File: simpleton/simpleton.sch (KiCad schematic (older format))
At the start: 57 parts

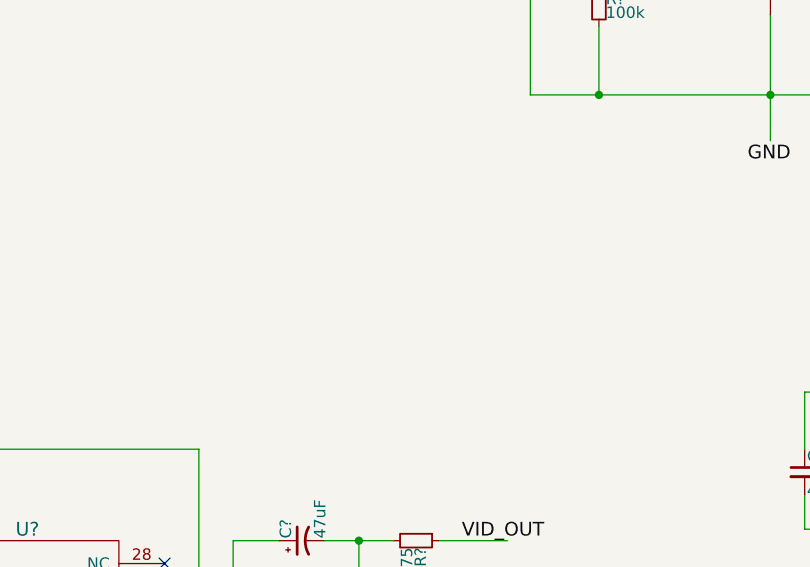
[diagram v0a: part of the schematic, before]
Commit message: Added vid ports and spek sat power port
Closes #13
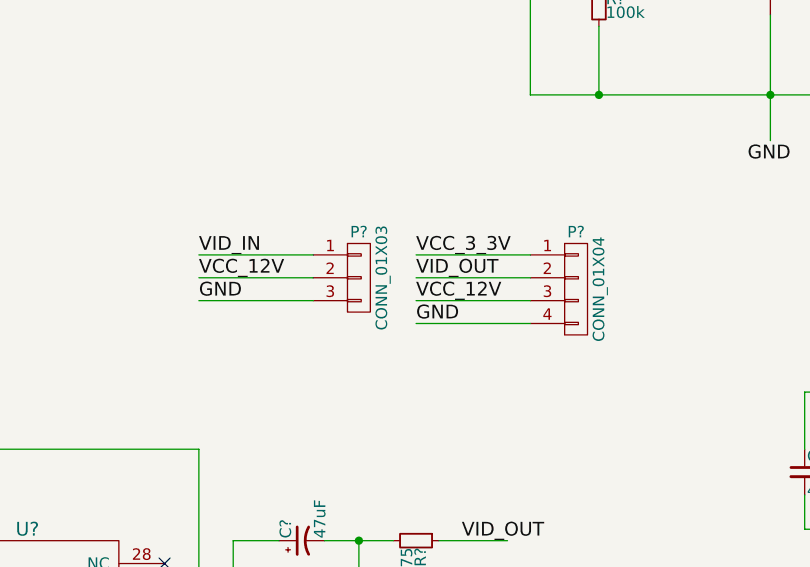
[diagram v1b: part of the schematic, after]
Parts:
- added P?: CONN_01X04, symbol CONN_01X04
- added P?: CONN_01X03, symbol CONN_01X03
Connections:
- net labels added: VCC_12V
- wire segments 228 -> 235
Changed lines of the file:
@@
 Text Label 800  1500 0    60   ~ 0
 U4_INV
+$Comp
+L CONN_01X04 P?
+U 1 1 56D50EB3
+P 11950 8350
+F 0 "P?" H 11950 8600 50  0000 C CNN
+F 1 "CONN_01X04" V 12050 8350 50  0000 C CNN
+F 2 "" H 11950 8350 60  0000 C CNN
+F 3 "" H 11950 8350 60  0000 C CNN
+	1    11950 8350
+	1    0    0    -1
+$EndComp
+Wire Wire Line
+	11750 8200 11250 8200
+Wire Wire Line
+	11750 8300 11250 8300
+Wire Wire Line
+	11750 8400 11250 8400
+Wire Wire Line
+	11750 8500 11250 8500
+Text Label 11250 8500 0    60   ~ 0
+GND
+Text Label 11250 8400 0    60   ~ 0
+VCC_12V
+Text Label 11250 8300 0    60   ~ 0
+VID_OUT
+Text Label 11250 8200 0    60   ~ 0
+VCC_3_3V
+$Comp
+L CONN_01X03 P?
+U 1 1 56D51B48
+P 11000 8300
+F 0 "P?" H 11000 8500 50  0000 C CNN
+F 1 "CONN_01X03" V 11100 8300 50  0000 C CNN
+F 2 "" H 11000 8300 60  0000 C CNN
+F 3 "" H 11000 8300 60  0000 C CNN
+	1    11000 8300
+	1    0    0    -1
+$EndComp
+Wire Wire Line
+	10800 8400 10300 8400
+Wire Wire Line
+	10800 8300 10300 8300
+Wire Wire Line
+	10800 8200 10300 8200
+Text Label 10300 8400 0    60   ~ 0
+GND
+Text Label 10300 8300 0    60   ~ 0
+VCC_12V
+Text Label 10300 8200 0    60   ~ 0
+VID_IN
 $EndSCHEMATC

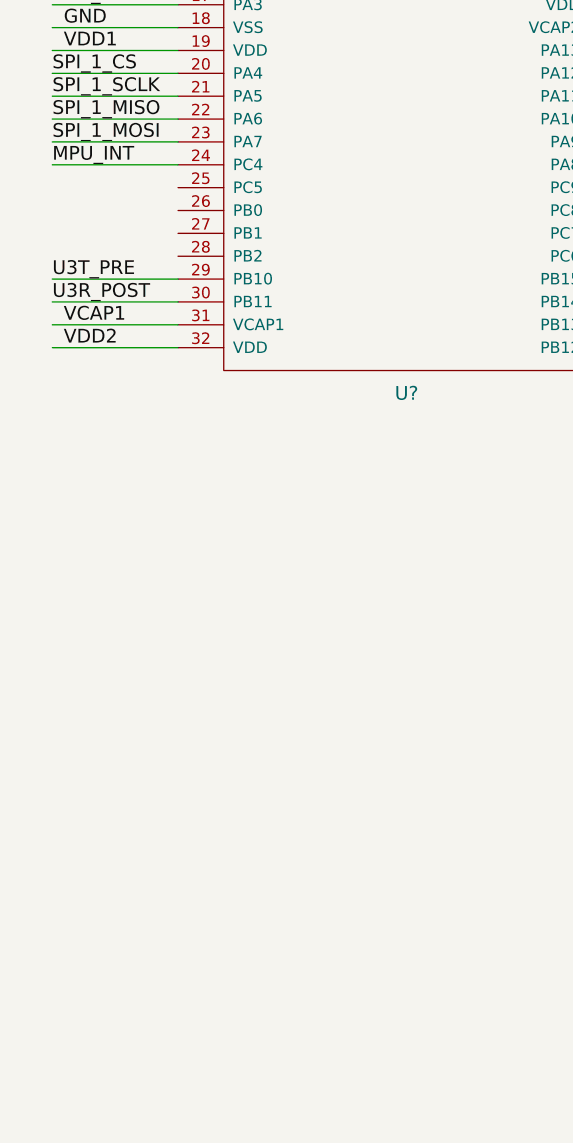
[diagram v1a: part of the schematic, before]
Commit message: Added ESC outputs
Closes #9
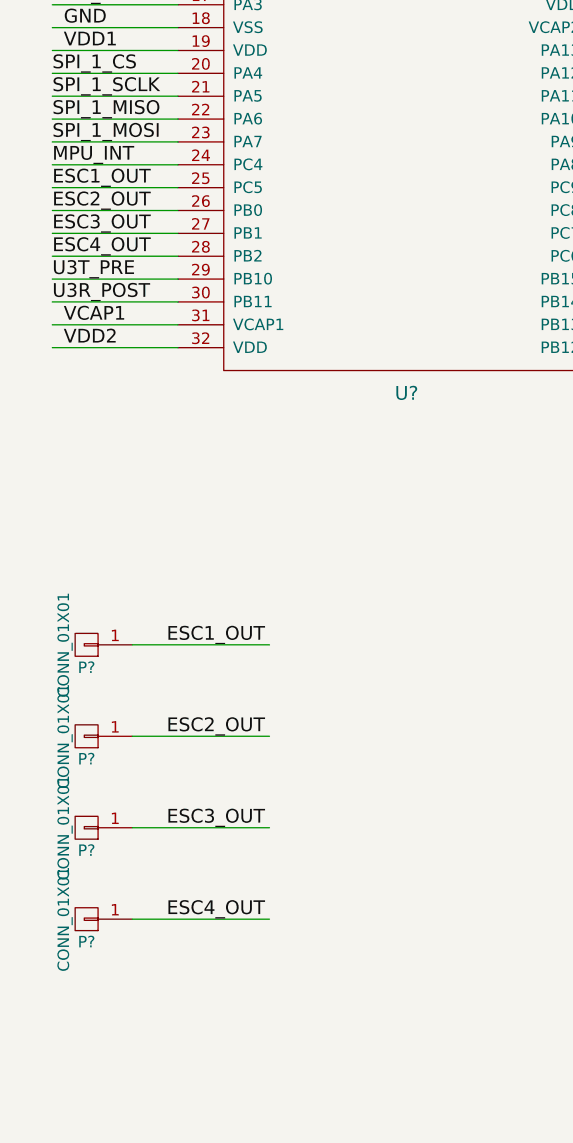
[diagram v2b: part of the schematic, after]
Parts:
- added P? (x4): CONN_01X01, symbol CONN_01X01
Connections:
- net labels added: ESC1_OUT, ESC2_OUT, ESC3_OUT, ESC4_OUT
- wire segments 235 -> 243
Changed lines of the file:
@@
 Text Label 10300 8200 0    60   ~ 0
 VID_IN
+$Comp
+L CONN_01X01 P?
+U 1 1 56D52A66
+P 950 5600
+F 0 "P?" H 950 5700 50  0000 C CNN
+F 1 "CONN_01X01" V 1050 5600 50  0000 C CNN
+F 2 "" H 950 5600 60  0000 C CNN
+F 3 "" H 950 5600 60  0000 C CNN
+	1    950  5600
+	-1   0    0    1
+$EndComp
+Wire Wire Line
+	1150 5600 1750 5600
+Text Label 1300 5600 0    60   ~ 0
+ESC1_OUT
+$Comp
+L CONN_01X01 P?
+U 1 1 56D52E15
+P 950 6000
+F 0 "P?" H 950 6100 50  0000 C CNN
+F 1 "CONN_01X01" V 1050 6000 50  0000 C CNN
+F 2 "" H 950 6000 60  0000 C CNN
+F 3 "" H 950 6000 60  0000 C CNN
+	1    950  6000
+	-1   0    0    1
+$EndComp
+Wire Wire Line
+	1150 6000 1750 6000
+Text Label 1300 6000 0    60   ~ 0
+ESC2_OUT
+$Comp
+L CONN_01X01 P?
+U 1 1 56D53219
+P 950 6400
+F 0 "P?" H 950 6500 50  0000 C CNN
+F 1 "CONN_01X01" V 1050 6400 50  0000 C CNN
+F 2 "" H 950 6400 60  0000 C CNN
+F 3 "" H 950 6400 60  0000 C CNN
+	1    950  6400
+	-1   0    0    1
+$EndComp
+Wire Wire Line
+	1150 6400 1750 6400
+Text Label 1300 6400 0    60   ~ 0
+ESC3_OUT
+$Comp
+L CONN_01X01 P?
+U 1 1 56D53518
+P 950 6800
+F 0 "P?" H 950 6900 50  0000 C CNN
+F 1 "CONN_01X01" V 1050 6800 50  0000 C CNN
+F 2 "" H 950 6800 60  0000 C CNN
+F 3 "" H 950 6800 60  0000 C CNN
+	1    950  6800
+	-1   0    0    1
+$EndComp
+Wire Wire Line
+	1150 6800 1750 6800
+Text Label 1300 6800 0    60   ~ 0
+ESC4_OUT
+Wire Wire Line
+	1350 3600 800  3600
+Wire Wire Line
+	1350 3700 800  3700
+Wire Wire Line
+	1350 3800 800  3800
+Wire Wire Line
+	1350 3900 800  3900
+Text Label 800  3600 0    60   ~ 0
+ESC1_OUT
+Text Label 800  3700 0    60   ~ 0
+ESC2_OUT
+Text Label 800  3800 0    60   ~ 0
+ESC3_OUT
+Text Label 800  3900 0    60   ~ 0
+ESC4_OUT
 $EndSCHEMATC

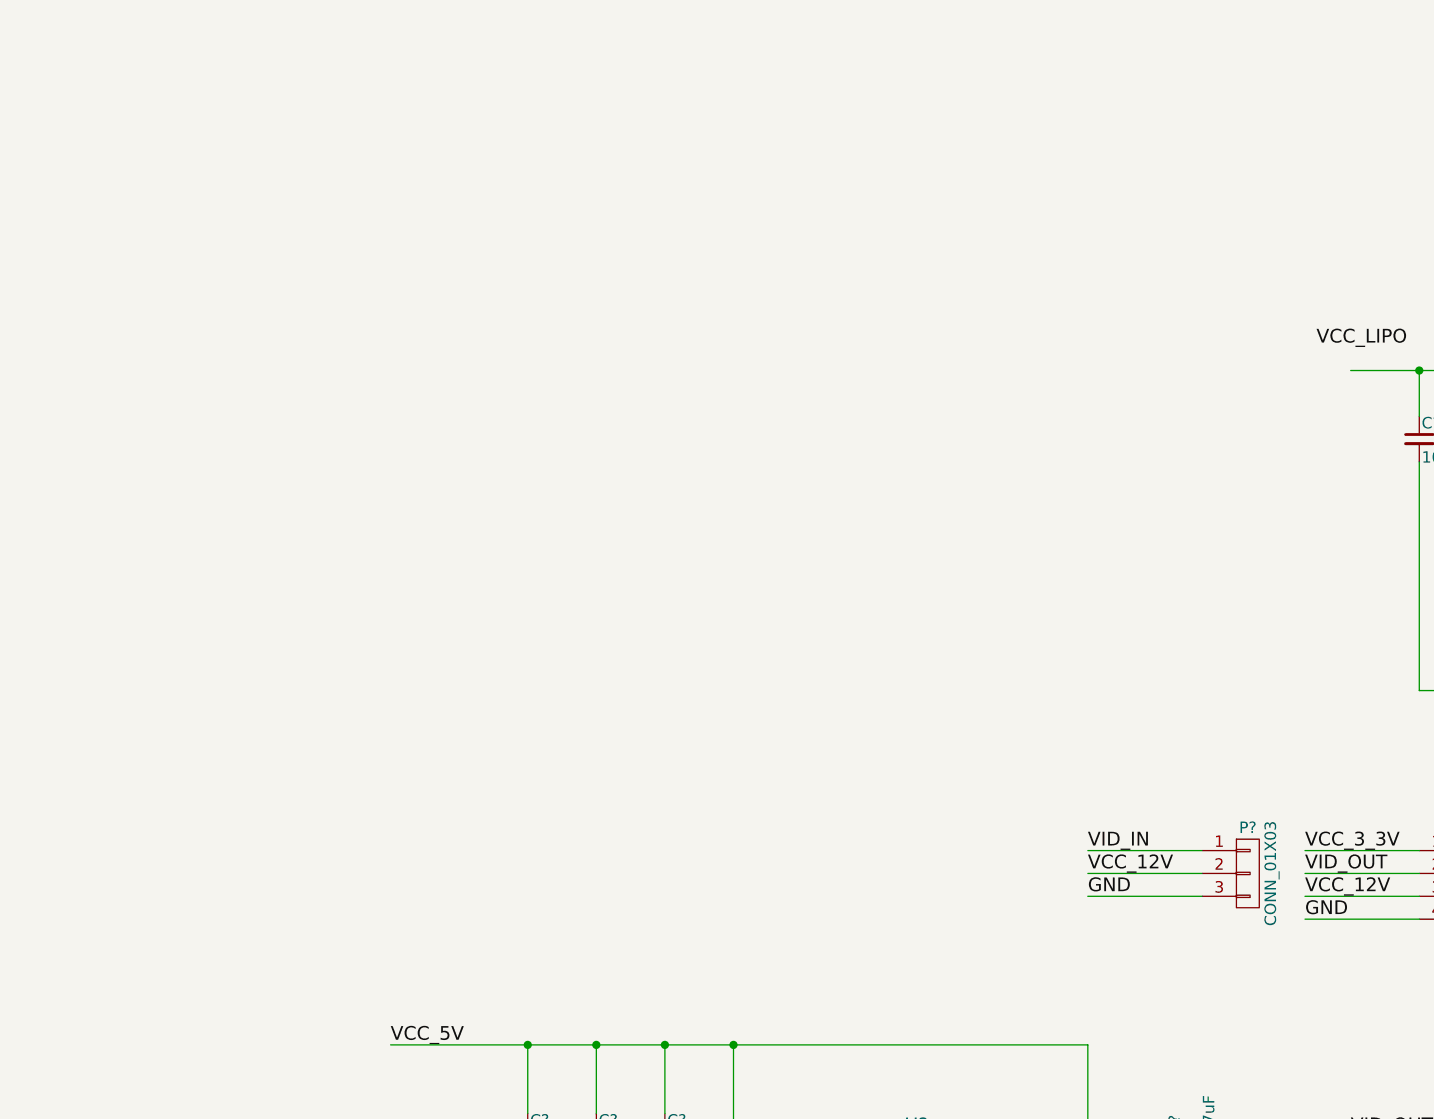
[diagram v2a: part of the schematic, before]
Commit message: Added 9/12V regulator
Closes #10

- Added regulator for 9/12V
- Added jumper for for voltage selection
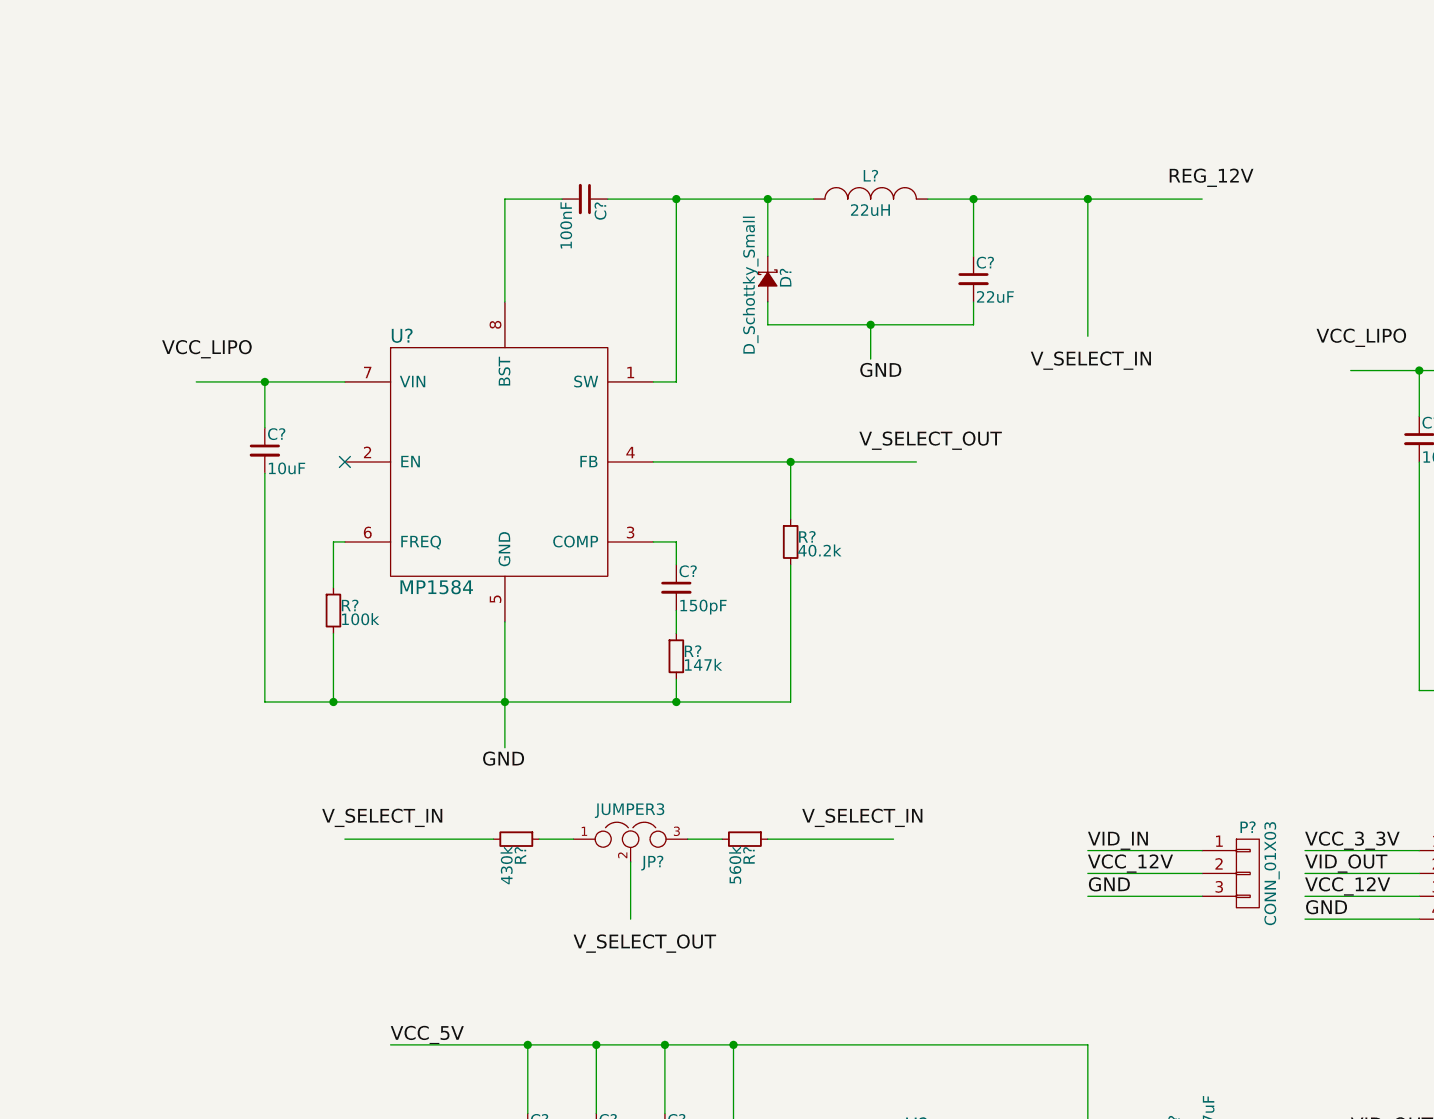
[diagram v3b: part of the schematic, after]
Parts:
- added C?: 10uF, symbol C_Small
- added C?: 150pF, symbol C_Small
- added C?: 100nF, symbol C_Small
- added C?: 22uF, symbol C_Small
- added D?: D_Schottky_Small, symbol D_Schottky_Small
- added JP?: JUMPER3, symbol JUMPER3
- added L?: 22uH, symbol INDUCTOR_SMALL
- added R?: 100k, symbol R_Small
- added R?: 147k, symbol R_Small
- added R?: 40.2k, symbol R_Small
- added R?: 560k, symbol R_Small
- added R?: 430k, symbol R_Small
- added U?: MP1584, symbol MP1584
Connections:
- net labels added: REG_12V, V_SELECT_IN, V_SELECT_OUT
- wire segments 243 -> 276
- no-connect marks 39 -> 40

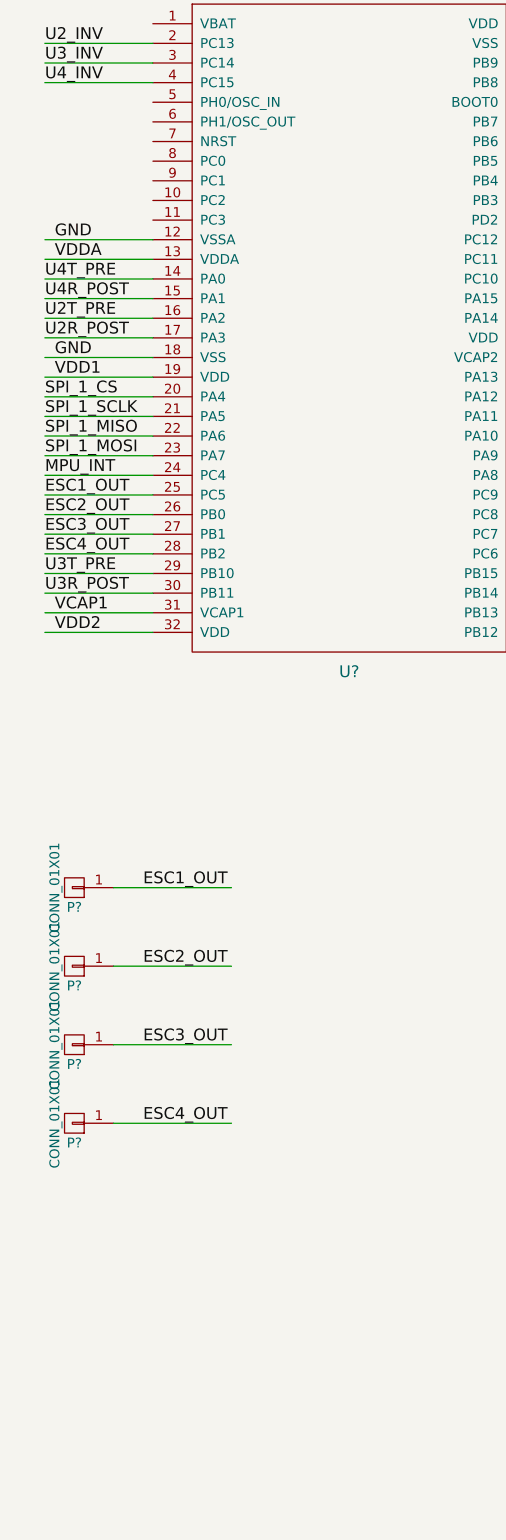
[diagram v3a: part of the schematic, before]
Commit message: Added voltage divider
Closes #12

- R1 = 70k, R2 = 10k
- Supports HV 6S operation
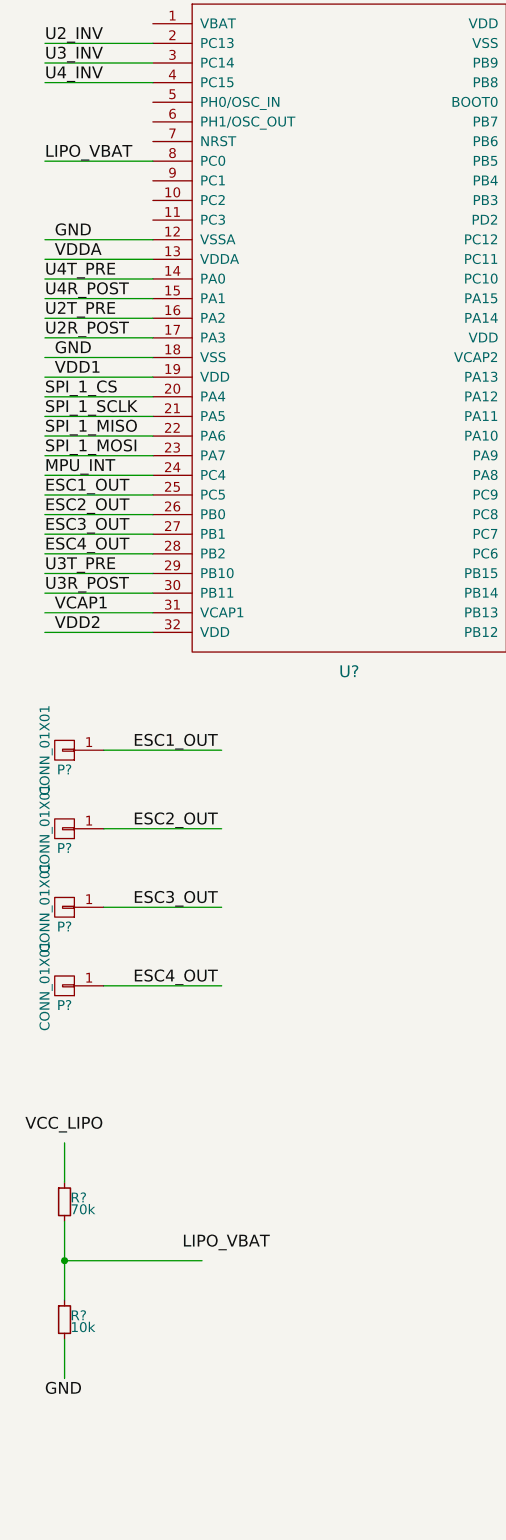
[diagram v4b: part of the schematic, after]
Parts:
- added R?: 70k, symbol R_Small
- added R?: 10k, symbol R_Small
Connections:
- net labels added: LIPO_VBAT
- wire segments 276 -> 281
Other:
- moved on the sheet: P?
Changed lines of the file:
@@
 L CONN_01X01 P?
 U 1 1 56D52A66
-P 950 5600
-F 0 "P?" H 950 5700 50  0000 C CNN
-F 1 "CONN_01X01" V 1050 5600 50  0000 C CNN
-F 2 "" H 950 5600 60  0000 C CNN
-F 3 "" H 950 5600 60  0000 C CNN
-	1    950  5600
+P 900 4900
+F 0 "P?" H 900 5000 50  0000 C CNN
+F 1 "CONN_01X01" V 1000 4900 50  0000 C CNN
+F 2 "" H 900 4900 60  0000 C CNN
+F 3 "" H 900 4900 60  0000 C CNN
+	1    900  4900
 	-1   0    0    1
 $EndComp
-Text Label 1300 5600 0    60   ~ 0
+Text Label 1250 4900 0    60   ~ 0
 ESC1_OUT
 $Comp
 L CONN_01X01 P?
 U 1 1 56D52E15
-P 950 6000
-F 0 "P?" H 950 6100 50  0000 C CNN
-F 1 "CONN_01X01" V 1050 6000 50  0000 C CNN
-F 2 "" H 950 6000 60  0000 C CNN
-F 3 "" H 950 6000 60  0000 C CNN
-	1    950  6000
+P 900 5300
+F 0 "P?" H 900 5400 50  0000 C CNN
+F 1 "CONN_01X01" V 1000 5300 50  0000 C CNN
+F 2 "" H 900 5300 60  0000 C CNN
+F 3 "" H 900 5300 60  0000 C CNN
+	1    900  5300
 	-1   0    0    1
 $EndComp
-Text Label 1300 6000 0    60   ~ 0
+Text Label 1250 5300 0    60   ~ 0
 ESC2_OUT
 $Comp
 L CONN_01X01 P?
 U 1 1 56D53219
-P 950 6400
-F 0 "P?" H 950 6500 50  0000 C CNN
-F 1 "CONN_01X01" V 1050 6400 50  0000 C CNN
-F 2 "" H 950 6400 60  0000 C CNN
-F 3 "" H 950 6400 60  0000 C CNN
-	1    950  6400
+P 900 5700
+F 0 "P?" H 900 5800 50  0000 C CNN
+F 1 "CONN_01X01" V 1000 5700 50  0000 C CNN
+F 2 "" H 900 5700 60  0000 C CNN
+F 3 "" H 900 5700 60  0000 C CNN
+	1    900  5700
 	-1   0    0    1
 $EndComp
-Text Label 1300 6400 0    60   ~ 0
+Text Label 1250 5700 0    60   ~ 0
 ESC3_OUT
 $Comp
 L CONN_01X01 P?
 U 1 1 56D53518
-P 950 6800
-F 0 "P?" H 950 6900 50  0000 C CNN
-F 1 "CONN_01X01" V 1050 6800 50  0000 C CNN
-F 2 "" H 950 6800 60  0000 C CNN
-F 3 "" H 950 6800 60  0000 C CNN
-	1    950  6800
+P 900 6100
+F 0 "P?" H 900 6200 50  0000 C CNN
+F 1 "CONN_01X01" V 1000 6100 50  0000 C CNN
+F 2 "" H 900 6100 60  0000 C CNN
+F 3 "" H 900 6100 60  0000 C CNN
+	1    900  6100
 	-1   0    0    1
 $EndComp
-Text Label 1300 6800 0    60   ~ 0
+Text Label 1250 6100 0    60   ~ 0
 ESC4_OUT
 Text Label 800  3600 0    60   ~ 0
@@
 	10800 8200 10300 8200
 Wire Wire Line
-	1150 5600 1750 5600
-Wire Wire Line
-	1150 6000 1750 6000
-Wire Wire Line
-	1150 6400 1750 6400
-Wire Wire Line
-	1150 6800 1750 6800
+	1100 4900 1700 4900
+Wire Wire Line
+	1100 5300 1700 5300
+Wire Wire Line
+	1100 5700 1700 5700
+Wire Wire Line
+	1100 6100 1700 6100
 Wire Wire Line
 	1350 3600 800  3600
@@
 Text Label 6950 8100 0    60   ~ 0
 V_SELECT_IN
+$Comp
+L R_Small R?
+U 1 1 56D558A9
+P 900 7200
+F 0 "R?" H 930 7220 50  0000 L CNN
+F 1 "70k" H 930 7160 50  0000 L CNN
+F 2 "" H 900 7200 60  0000 C CNN
+F 3 "" H 900 7200 60  0000 C CNN
+	1    900  7200
+	1    0    0    -1
+$EndComp
+Wire Wire Line
+	900  7300 900  7700
+Wire Wire Line
+	900  7500 1600 7500
+Connection ~ 900  7500
+$Comp
+L R_Small R?
+U 1 1 56D55CF9
+P 900 7800
+F 0 "R?" H 930 7820 50  0000 L CNN
+F 1 "10k" H 930 7760 50  0000 L CNN
+F 2 "" H 900 7800 60  0000 C CNN
+F 3 "" H 900 7800 60  0000 C CNN
+	1    900  7800
+	1    0    0    -1
+$EndComp
+Wire Wire Line
+	900  7900 900  8100
+Wire Wire Line
+	900  7100 900  6900
+Text Label 700  6850 0    60   ~ 0
+VCC_LIPO
+Text Label 800  8200 0    60   ~ 0
+GND
+Text Label 1500 7450 0    60   ~ 0
+LIPO_VBAT
+Wire Wire Line
+	1350 1900 800  1900
+Text Label 800  1900 0    60   ~ 0
+LIPO_VBAT
 $EndSCHEMATC
